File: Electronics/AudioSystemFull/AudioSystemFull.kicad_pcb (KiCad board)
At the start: 2 copper layers, 232.1 x 165.7 mm, 303 parts, among them IC1 TDA1558Q, J1 SJ1-3515-SMT-TR-BE, J3 Conn_Display_Buttons, J6 Conn_ISO, U1 MIC39100-5.0WS, U10 LT3015EQ-5PBF, U11 OPA2134, U12 OPA2134, U13 OPA2134, U14 OPA2134, U15 OPA2134, U16 OPA2134, U17 OPA2134, U18 OPA2134, U19 OPA2134, U2 DEVKIT_V1_ESP32-WROOM-32, U20 OPA2134, U21 OPA2134, U22 OPA2134, U23 OPA2134, U24 OPA2134, U25 OPA2134, U26 OPA2134, U27 OPA2134, U28 OPA2134, U3 PCM5102A, U4 OPA2134, U5 LP5907MFX-3.3, U6 LMR51420YFDDCR, U7 LMR51420YFDDCR, U8 LP5907MFX-3.3, U9 LMR51420YFDDCR

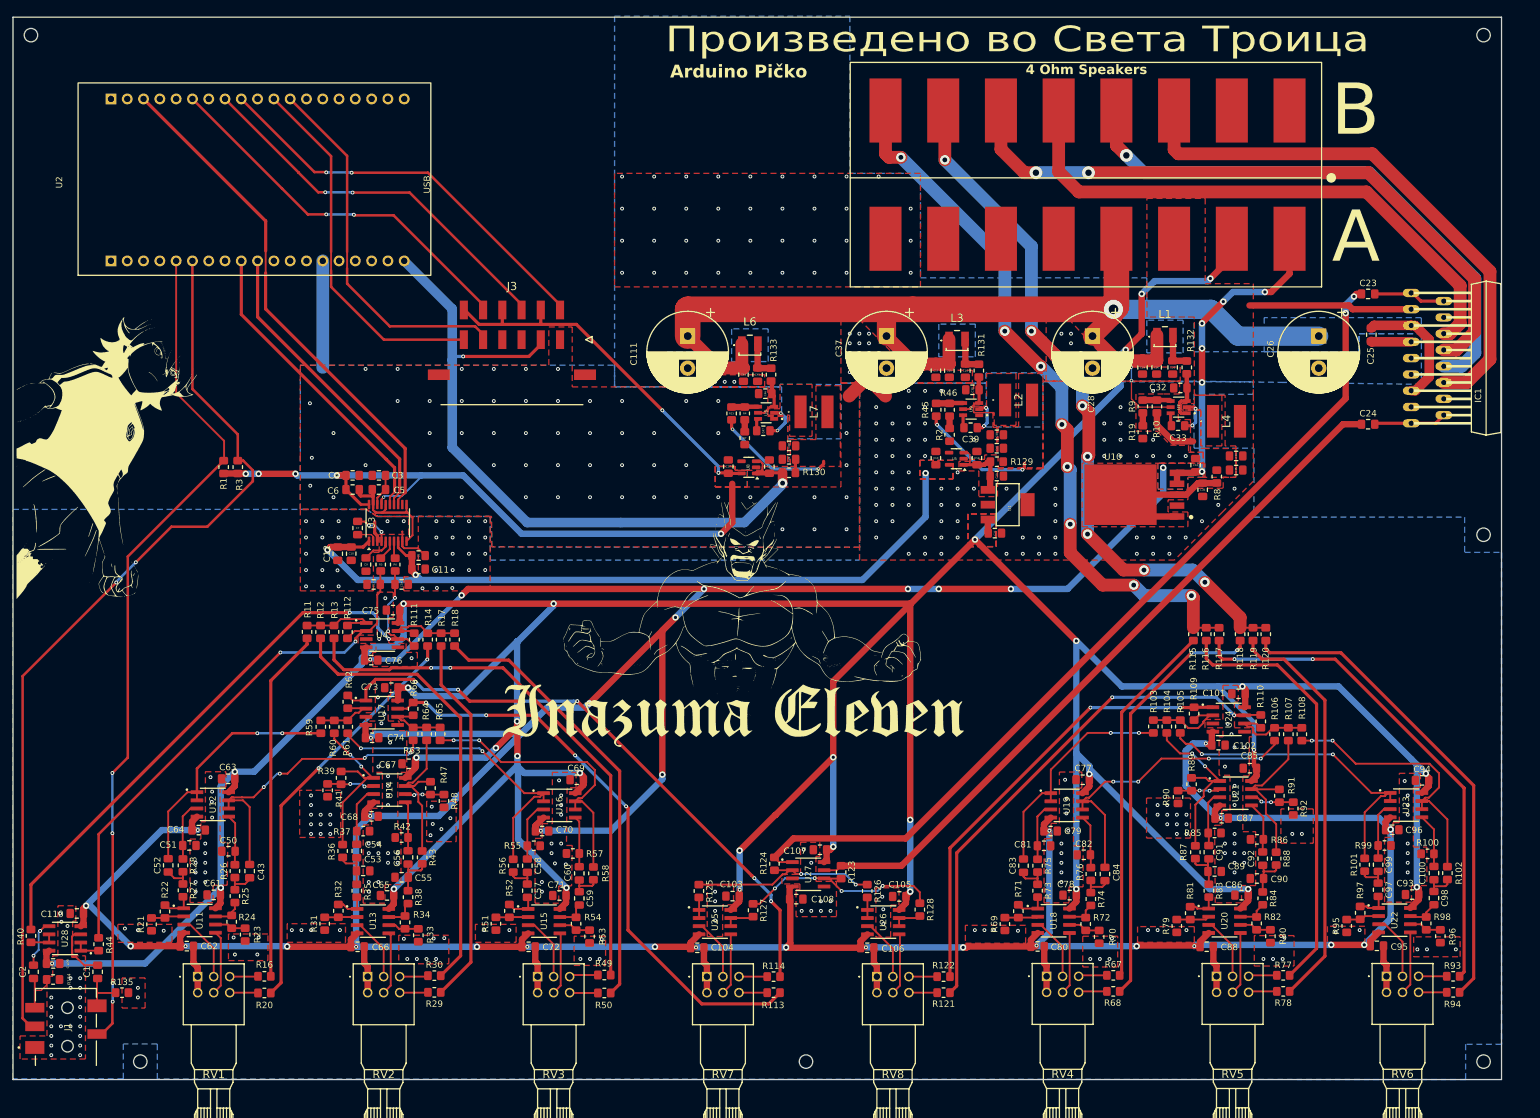
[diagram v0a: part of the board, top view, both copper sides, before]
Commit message: add mounting holes to main pcb
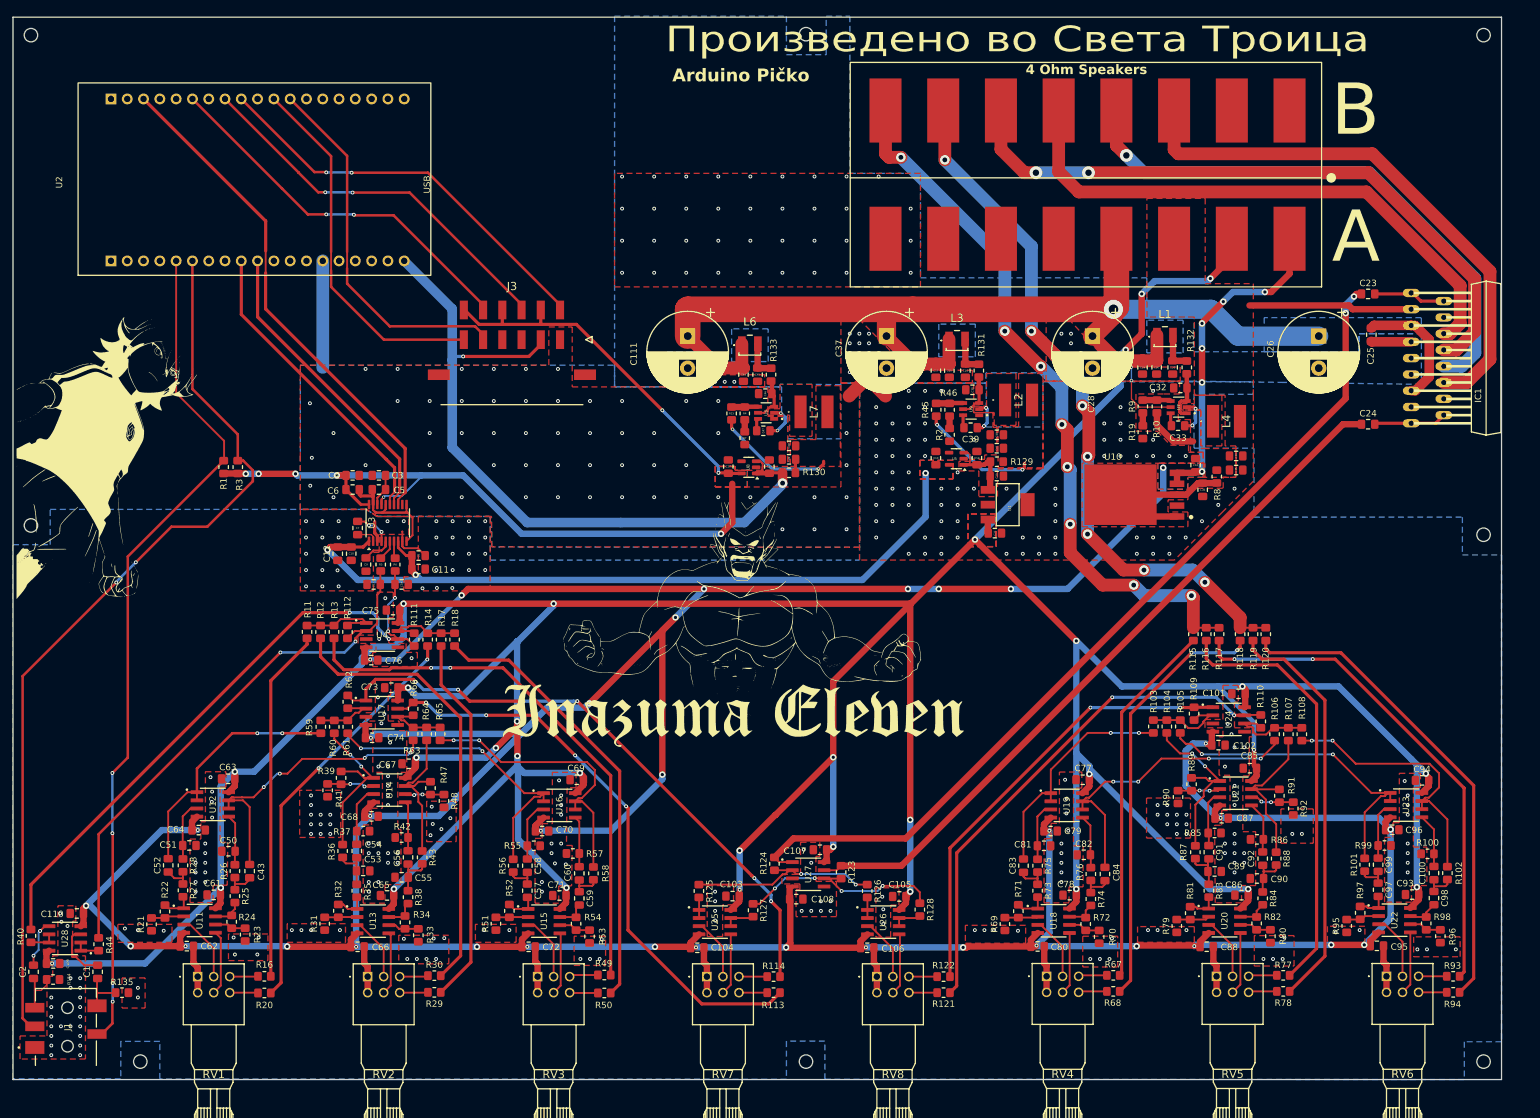
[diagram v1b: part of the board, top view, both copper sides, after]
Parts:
- added REF**: MountingHole_2.1mm, MountingHole:MountingHole_2.1mm, F.Cu at (283.9, 147.8)
- added REF**: MountingHole_2.1mm, MountingHole:MountingHole_2.1mm, F.Cu at (163.0, 224.4)
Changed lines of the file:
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@@
 		)
 	)
+	(footprint "MountingHole:MountingHole_2.1mm"
+		(layer "F.Cu")
+		(at 283.85 147.8)
+		(descr "Mounting Hole 2.1mm, no annular")
+		(tags "mounting hole 2.1mm no annular")
+		(property "Reference" "REF**"
+			(at 0 -3.2 0)
+			(layer "F.SilkS")
+			(hide yes)
+			(effects
+				(font
+					(size 1 1)
+					(thickness 0.15)
+				)
+			)
+		)
+		(property "Value" "MountingHole_2.1mm"
+			(at 0 3.2 0)
+			(layer "F.Fab")
+			(effects
+				(font
+					(size 1 1)
+					(thickness 0.15)
+				)
+			)
+		)
+		(property "Footprint" "MountingHole:MountingHole_2.1mm"
+			(at 0 0 0)
+			(unlocked yes)
+			(layer "F.Fab")
+			(hide yes)
+			(effects
+				(font
+					(size 1.27 1.27)
+					(thickness 0.15)
+				)
+			)
+		)
+		(property "Datasheet" ""
+			(at 0 0 0)
+			(unlocked yes)
+			(layer "F.Fab")
+			(hide yes)
+			(effects
+				(font
+					(size 1.27 1.27)
+					(thickness 0.15)
+				)
+			)
+		)
+		(property "Description" ""
+			(at 0 0 0)
+			(unlocked yes)
+			(layer "F.Fab")
+			(hide yes)
+			(effects
+				(font
+					(size 1.27 1.27)
+					(thickness 0.15)
+				)
+			)
+		)
+		(attr exclude_from_pos_files exclude_from_bom)
+		(fp_circle
+			(center 0 0)
+			(end 2.1 0)
+			(stroke
+				(width 0.15)
+				(type solid)
+			)
+			(fill none)
+			(layer "Cmts.User")
+		)
+		(fp_circle
+			(center 0 0)
+			(end 2.35 0)
+			(stroke
+				(width 0.05)
+				(type solid)
+			)
+			(fill none)
+			(layer "F.CrtYd")
+		)
+		(fp_text user "${REFERENCE}"
+			(at 0 0 0)
+			(layer "F.Fab")
+			(effects
+				(font
+					(size 1 1)
+					(thickness 0.15)
+				)
+			)
+		)
+		(pad "" np_thru_hole circle
+			(at 0 0)
+			(size 2.1 2.1)
+			(drill 2.1)
+			(layers "F&B.Cu" "*.Mask")
+		)
+	)
 	(footprint "Capacitor_SMD:C_0805_2012Metric_Pad1.18x1.45mm_HandSolder"
 		(layer "F.Cu")
@@
 		)
 	)
+	(footprint "MountingHole:MountingHole_2.1mm"
+		(layer "F.Cu")
+		(at 163 224.4)
+		(descr "Mounting Hole 2.1mm, no annular")
+		(tags "mounting hole 2.1mm no annular")
+		(property "Reference" "REF**"
+			(at 0 -3.2 0)
+			(layer "F.SilkS")
+			(hide yes)
+			(effects
+				(font
+					(size 1 1)
+					(thickness 0.15)
+				)
+			)
+		)
+		(property "Value" "MountingHole_2.1mm"
+			(at 0 3.2 0)
+			(layer "F.Fab")
+			(effects
+				(font
+					(size 1 1)
+					(thickness 0.15)
+				)
+			)
+		)
+		(property "Footprint" "MountingHole:MountingHole_2.1mm"
+			(at 0 0 0)
+			(unlocked yes)
+			(layer "F.Fab")
+			(hide yes)
+			(effects
+				(font
+					(size 1.27 1.27)
+					(thickness 0.15)
+				)
+			)
+		)
+		(property "Datasheet" ""
+			(at 0 0 0)
+			(unlocked yes)
+			(layer "F.Fab")
+			(hide yes)
+			(effects
+				(font
+					(size 1.27 1.27)
+					(thickness 0.15)
+				)
+			)
+		)
+		(property "Description" ""
+			(at 0 0 0)
+			(unlocked yes)
+			(layer "F.Fab")
+			(hide yes)
+			(effects
+				(font
+					(size 1.27 1.27)
+					(thickness 0.15)
+				)
+			)
+		)
+		(attr exclude_from_pos_files exclude_from_bom)
+		(fp_circle
+			(center 0 0)
+			(end 2.1 0)
+			(stroke
+				(width 0.15)
+				(type solid)
+			)
+			(fill none)
+			(layer "Cmts.User")
+		)
+		(fp_circle
+			(center 0 0)
+			(end 2.35 0)
+			(stroke
+				(width 0.05)
+				(type solid)
+			)
+			(fill none)
+			(layer "F.CrtYd")
+		)
+		(fp_text user "${REFERENCE}"
+			(at 0 0 0)
+			(layer "F.Fab")
+			(effects
+				(font
+					(size 1 1)
+					(thickness 0.15)
+				)
+			)
+		)
+		(pad "" np_thru_hole circle
+			(at 0 0)
+			(size 2.1 2.1)
+			(drill 2.1)
+			(layers "F&B.Cu" "*.Mask")
+		)
+	)
 	(footprint "Resistor_SMD:R_0805_2012Metric_Pad1.20x1.40mm_HandSolder"
 		(layer "F.Cu")
@@
 	)
 	(gr_text "Arduino Pičko\n"
-		(at 262.65 154.8 0)
+		(at 263 155.4 0)
 		(layer "F.SilkS")
 		(effects
@@
 				(xy 379.8 194.5) (xy 379.8 202.4) (xy 358.3 202.1) (xy 344.2 201.9) (xy 332.75 201.9) (xy 321.3 201.9)
 				(xy 321.3 200.6) (xy 316.6 200.6) (xy 311.9 200.6) (xy 311.9 202.2) (xy 289.3 202.2) (xy 289.3 202.45)
-				(xy 284.8 202.4) (xy 279.8 202.4) (xy 279.8 202.8) (xy 254 202.8) (xy 254 145) (xy 290.7 145)
+				(xy 284.8 202.4) (xy 279.8 202.4) (xy 279.8 202.8) (xy 254 202.8) (xy 254 145) (xy 280.8 145) (xy 280.8 151)
+				(xy 287 151) (xy 287 145) (xy 290.7 145)
 			)
 		)
@@
 		(polygon
 			(pts
-				(xy 337 192.4) (xy 337 197.5) (xy 342.65 197.5) (xy 342.65 192.4)
+				(xy 337 197.5) (xy 342.65 197.5) (xy 342.65 192.4) (xy 337 192.4)
 			)
 		)
@@
 		(polygon
 			(pts
-				(xy 353.6 203.95) (xy 344.35 203.95) (xy 344.35 212.35) (xy 353.7 212.35) (xy 353.7 223.1) (xy 386.55 223.1)
-				(xy 386.55 228.6) (xy 392.3 228.6) (xy 392.3 262.9) (xy 392.3 291.566795) (xy 392.3 291.6) (xy 392.3 305.3)
-				(xy 386.7 305.3) (xy 386.7 310.797587) (xy 182.7 310.709586) (xy 182.7 305.25) (xy 177.4 305.25)
-				(xy 177.4 310.707518) (xy 160.2 310.7) (xy 160.2 221.9) (xy 215.3 221.9) (xy 217 223) (xy 234.6 223)
-				(xy 234.6 229.8) (xy 292.2 229.8) (xy 292.2 202.25) (xy 311.95 202.25) (xy 311.95 209.05) (xy 320.8 209.05)
-				(xy 320.8 202) (xy 353.6 202)
+				(xy 353.6 203.95) (xy 344.35 203.95) (xy 344.35 212.35) (xy 353.7 212.35) (xy 353.7 223.1) (xy 386.2 223.1)
+				(xy 386.2 229) (xy 392.3 229) (xy 392.3 262.9) (xy 392.3 291.566795) (xy 392.3 291.6) (xy 392.3 304.9)
+				(xy 386.5 304.9) (xy 386.5 310.797587) (xy 286.8 310.754406) (xy 286.8 304.8) (xy 280.8 304.8) (xy 280.8 310.751817)
+				(xy 183.1 310.709586) (xy 183.1 304.85) (xy 177 304.85) (xy 177 310.707518) (xy 160.2 310.7) (xy 160.2 227.4)
+				(xy 166 227.4) (xy 166 221.9) (xy 215.3 221.9) (xy 217 223) (xy 234.6 223) (xy 234.6 229.8) (xy 292.2 229.8)
+				(xy 292.2 202.25) (xy 311.95 202.25) (xy 311.95 209.05) (xy 320.8 209.05) (xy 320.8 202) (xy 353.6 202)
 			)
 		)
